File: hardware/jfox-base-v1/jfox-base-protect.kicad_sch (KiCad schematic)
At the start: 13 parts, among them J50 PWR 1 RH, J51 PWR 2 LH

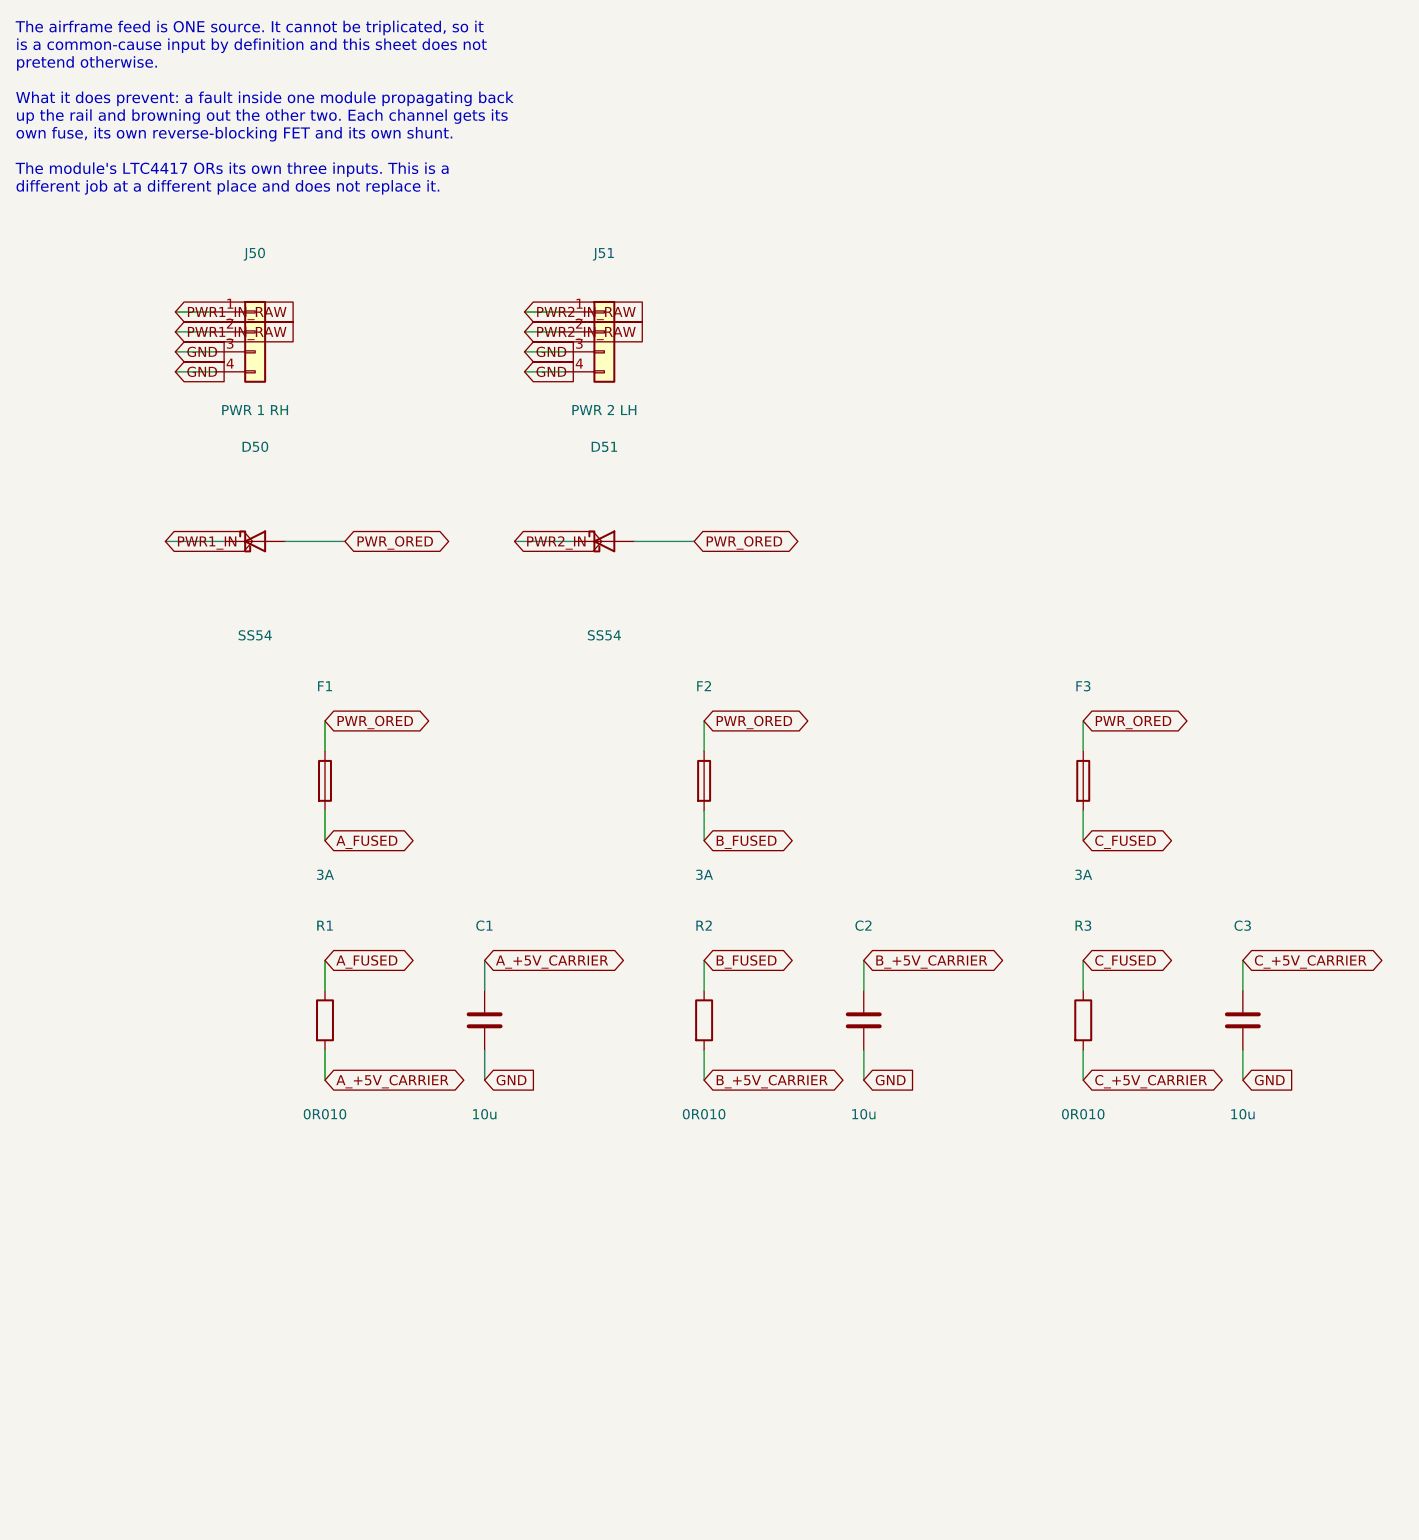
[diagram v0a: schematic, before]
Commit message: DO-160G protection stage, and a check that recognises parts not labels
Series inductance and an SMCJ clamp on each airframe feed, bulk on the ORed
rail, soft-start per slot. Order is deliberate - L, clamp, ORing, bulk - as
a TVS with nothing ahead of it absorbs the whole injected transient itself,
which is how a correctly chosen part still fails.

ASSUMED: section 22 pin injection LEVEL 3. It was not specified, so it is
recorded in the sheet note and in VOLTAGE_ANALYSIS.md rather than left
implicit. Level 4 or 5 need larger parts than these.

SECTION 16 POWER INTERRUPT IS NOT MET, and the arithmetic is why. Three
cards at 1.2 A riding 5.16 V down to 4.50 V need 1.8 mF for 1 ms and 364 mF
for 200 ms. 364 mF at 5 V is a supercapacitor bank. C60 is sized for the
feed-to-feed switchover the ORing stage itself creates, about 1 ms, and the
interrupt is declared not met. Meeting it means holding up at a higher
voltage ahead of the ORing or requiring the airframe to provide it - both
decisions above this board. Sizing for the case you can meet and letting the
requirement imply the other is how this goes wrong quietly.

D50/D51 retained. With the LTC4417's back-to-back pairs they are redundant
for SELECTION and cost ~0.4 V, but the pass FETs only block reverse current
in the orientation the controller drives them, and a feed connected
backwards is exactly the case where the controller has no say.

The check that verifies all this had the flaw this session keeps producing.
It tested `r.startswith("D")` - a reference designator prefix - so a board
whose clamps had been replaced by 0R resistors passed, because D60 was still
called D60. A refdes is a label someone chose; the value is what gets
fitted. It now matches against known clamp families and inductance forms,
and the negative test fails on the right line.

The inductance matcher was wrong too on first attempt: it required a
trailing H, and inductance is written 10u on a BOM, not 10uH. It rejected
every real value and repo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
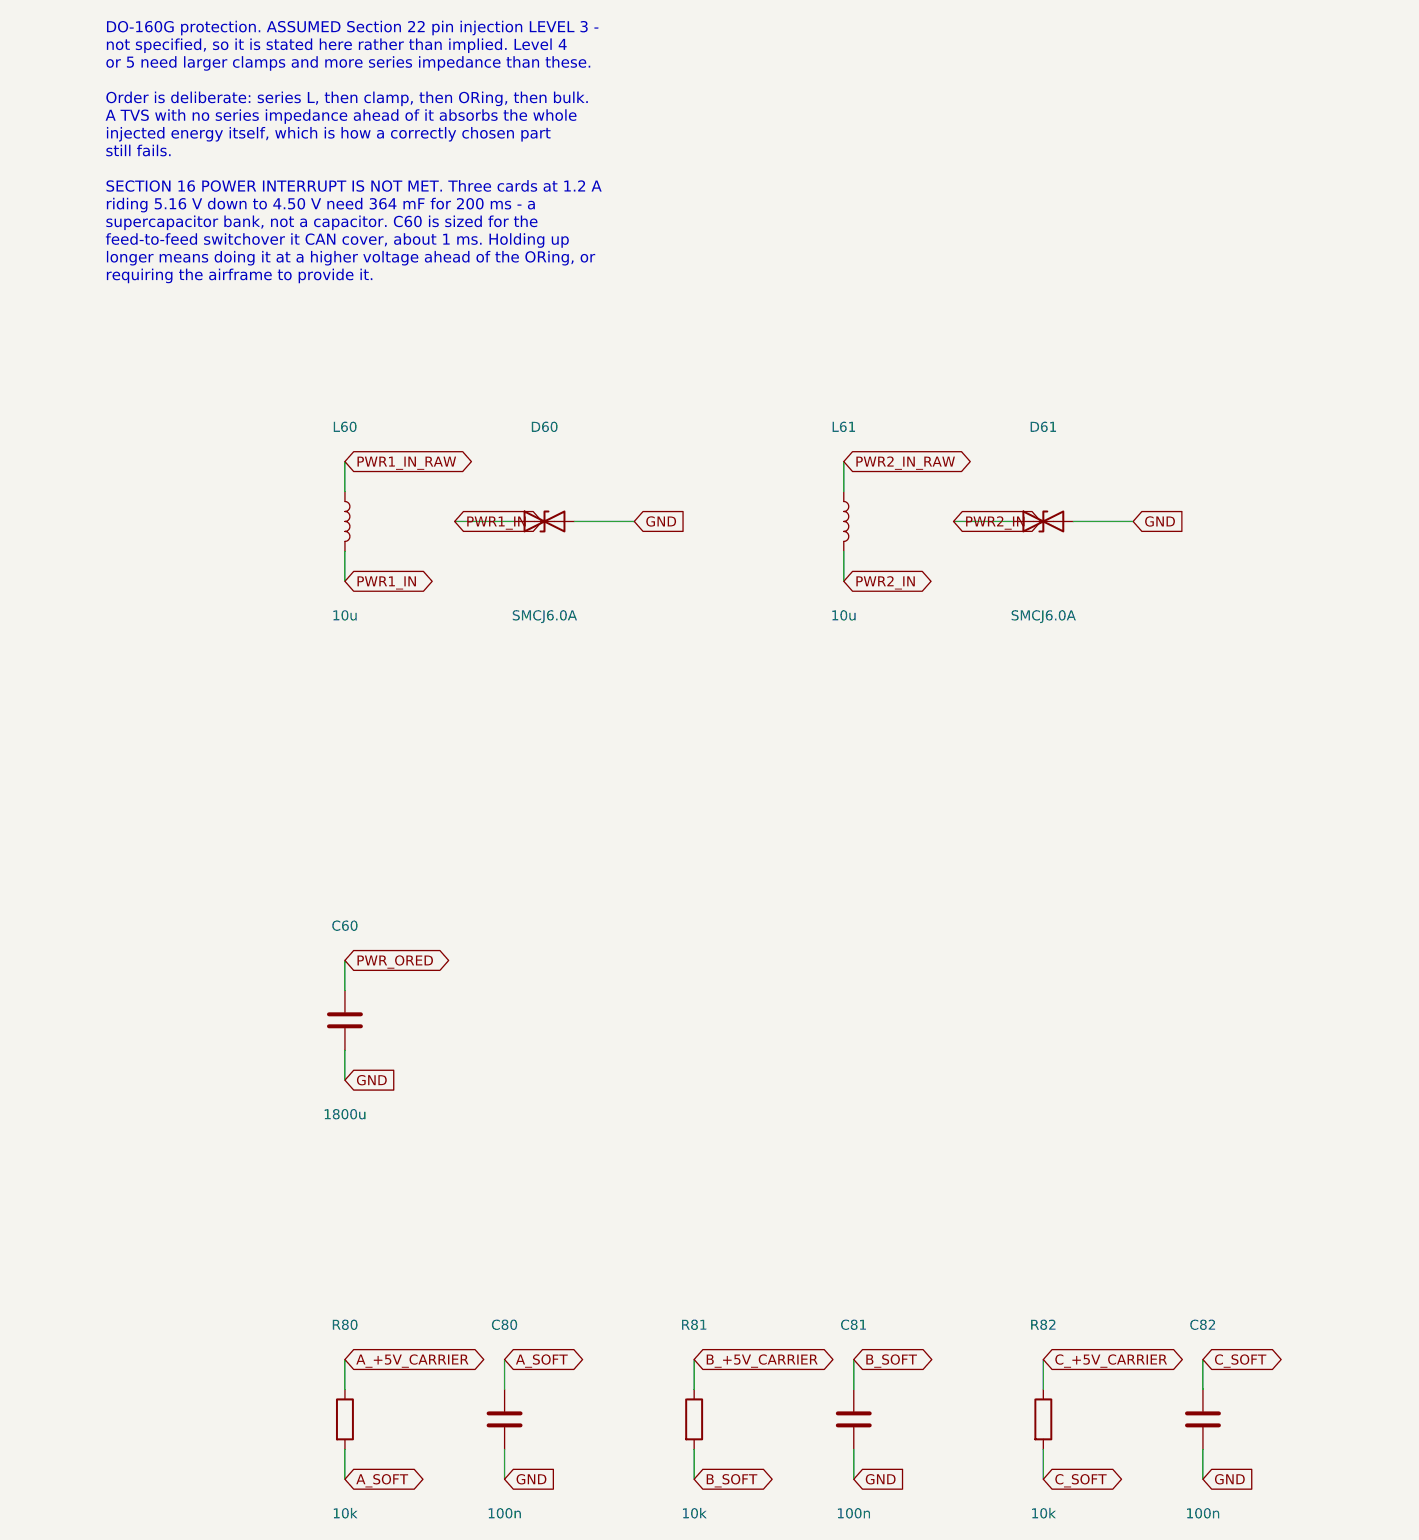
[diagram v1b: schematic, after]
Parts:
- removed C1, C2, C3: 10u, Capacitor_SMD:C_0805_2012Metric, symbol Device:C
- removed D50, D51: SS54, Diode_SMD:D_SMA, symbol Device:D_Schottky
- removed F1, F2, F3: 3A, Fuse:Fuse_1206_3216Metric, symbol Device:Fuse
- removed J50: PWR 1 RH, Connector_JST:JST_GH_SM04B-GHS-TB_1x04-1MP_P1.25mm_Horizontal, symbol Connector_Generic:Conn_01x04
- removed J51: PWR 2 LH, Connector_JST:JST_GH_SM04B-GHS-TB_1x04-1MP_P1.25mm_Horizontal, symbol Connector_Generic:Conn_01x04
- removed R1, R2, R3: 0R010, Resistor_SMD:R_0402_1005Metric, symbol Device:R
- added C60: 1800u, Capacitor_SMD:C_0402_1005Metric, symbol Device:C
- added C80, C81, C82: 100n, Capacitor_SMD:C_0402_1005Metric, symbol Device:C
- added D60, D61: SMCJ6.0A, Diode_SMD:D_SMC, symbol Device:D_TVS
- added L60, L61: 10u, Inductor_SMD:L_Bourns-SRN6045, symbol Device:L
- added R80, R81, R82: 10k, Resistor_SMD:R_0402_1005Metric, symbol Device:R
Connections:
- net A_+5V_CARRIER: now also R80.1
- net B_+5V_CARRIER: now also R81.1
- net C_+5V_CARRIER: now also R82.1
- net GND: now also C60.2, C80.2, C81.2, C82.2, D60.2 (A2), D61.2 (A2)
- net PWR1_IN: now also D60.1 (A1), L60.2
- net PWR1_IN_RAW: now also L60.1
- net PWR2_IN: now also D61.1 (A1), L61.2
- net PWR2_IN_RAW: now also L61.1
- net PWR_ORED: now also C60.1
- new net A_SOFT: C80.1, R80.2
- new net B_SOFT: C81.1, R81.2
- new net C_SOFT: C82.1, R82.2
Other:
- note added: "DO-160G protection. ASSUMED Section 22 pin injection LEVEL 3 - not specified, so it is stated here rather than implied. Level 4 or 5 need larger clamps and more series impedance than these. Order is deliberate: series L, then clamp, then ORing, then bulk. A TVS with no series impedance ahead of it absorbs the whole injected energy itself, which is how a correctly chosen part still fails. SECTION 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"
- note removed: "The airframe feed is ONE source. It cannot be triplicated, so it is a common-cause input by definition and this sheet does not pretend otherwise. What it does prevent: a fault inside one module propagating back up the rail and browning out the other two. Each channel gets its own fuse, its own reverse-blocking FET and its own shunt. The module's LTC4417 ORs its own three inputs. This is a differe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"
- title: Power distribution - per channel -> DO-160G protection - clamps, bulk, inrush
